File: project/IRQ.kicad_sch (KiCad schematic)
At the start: 6 parts, among them IC9 74HC148, SW5 NMI

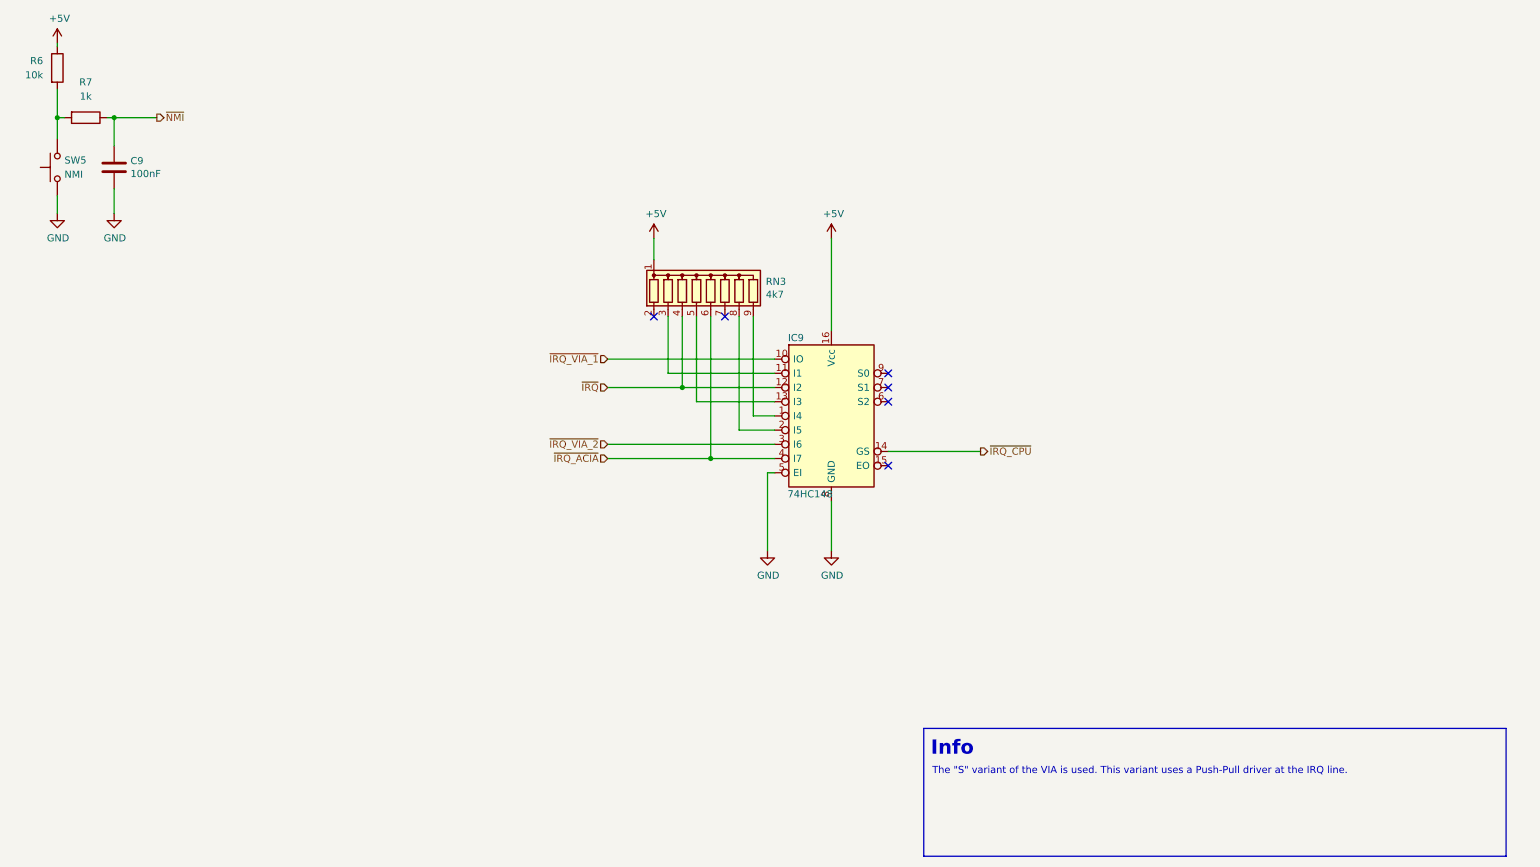
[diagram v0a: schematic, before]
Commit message: Fix grid issues, fix missing libraries, replace FT232 with FT231
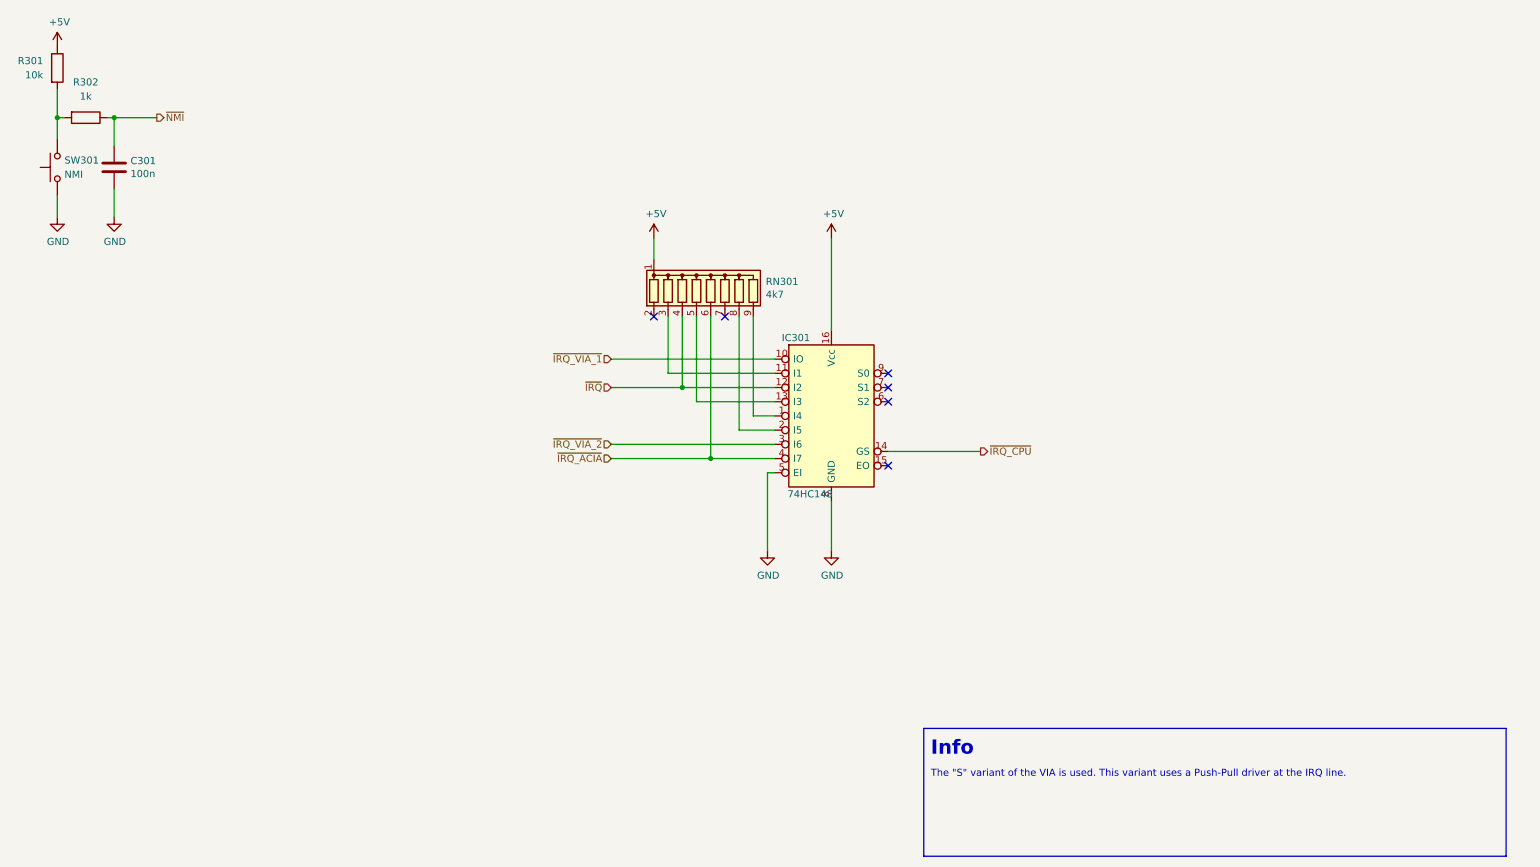
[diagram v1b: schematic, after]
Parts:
- C301: renamed from C9; value 100nF -> 100n
- renumbered IC9 to IC301, R6 to R301, R7 to R302, RN3 to RN301, SW5 to SW301

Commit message: Fix swapped DM and DP, add missing datasheets, remove Mouser property
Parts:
- C301: Mouser 810-FA18X8R1H104KRU6 -> (none)
- IC301: Mouser 595-SN74HC148N -> (none)
- R301: Mouser 603-MFP-25BRD52-10K -> (none)
- R302: Mouser 603-MFP-25BRD52-1K -> (none)
- RN301: Mouser 652-4609M-1LF-4.7K -> (none)
- SW301: Mouser 506-2-1825910-7 -> (none)
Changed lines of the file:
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@@
 			)
 		)
-		(property "Datasheet" "~"
+		(property "Datasheet" "https://www.mouser.de/datasheet/2/447/YAGEO_MFP_datasheet_2024v3-3447153.pdf"
 			(at 22.86 22.86 0)
 			(effects
@@
 		)
 		(property "Mfr. No." "MFP-25BRD52-10K"
-			(at 22.86 22.86 0)
-			(effects
-				(font
-					(size 1.27 1.27)
-				)
-				(hide yes)
-			)
-		)
-		(property "Mouser" "603-MFP-25BRD52-10K"
 			(at 22.86 22.86 0)
 			(effects
@@
 			)
 		)
-		(property "Datasheet" "~"
+		(property "Datasheet" "https://www.mouser.de/datasheet/2/418/7/ENG_CD_1825910_C10-2021098.pdf"
 			(at 17.78 40.64 0)
 			(effects
@@
 			)
 		)
-		(property "Mouser" "506-2-1825910-7"
-			(at 22.86 40.64 0)
-			(effects
-				(font
-					(size 1.27 1.27)
-				)
-				(hide yes)
-			)
-		)
 		(property "Distributor" "Mouser"
 			(at 22.86 40.64 0)
@@
 			)
 		)
-		(property "Datasheet" "~"
+		(property "Datasheet" "https://product.tdk.com/system/files/dam/doc/product/capacitor/ceramic/lead-mlcc/catalog/leadmlcc_halogenfree_fa150_en.pdf?ref_disty=mouser"
 			(at 33.02 40.64 0)
 			(effects
@@
 			)
 		)
-		(property "Mouser" "810-FA18X8R1H104KRU6"
-			(at 33.02 40.64 0)
-			(effects
-				(font
-					(size 1.27 1.27)
-				)
-				(hide yes)
-			)
-		)
 		(property "Distributor" "Mouser"
 			(at 33.02 40.64 0)
@@
 			)
 		)
-		(property "Mouser" "652-4609M-1LF-4.7K "
-			(at 139.7 62.23 0)
-			(effects
-				(font
-					(size 1.27 1.27)
-				)
-				(hide yes)
-			)
-		)
 		(property "Distributor" "Mouser"
 			(at 139.7 62.23 0)
@@
 		)
 		(property "Mfr. No." "SN74HC148N"
-			(at 161.29 85.09 0)
-			(effects
-				(font
-					(size 1.27 1.27)
-				)
-				(hide yes)
-			)
-		)
-		(property "Mouser" "595-SN74HC148N"
 			(at 161.29 85.09 0)
 			(effects
@@
 			)
 		)
-		(property "Datasheet" "~"
+		(property "Datasheet" "https://www.mouser.de/datasheet/2/447/Yageo_LR_MFP_1-1947926.pdf"
 			(at 27.94 31.75 0)
 			(effects
@@
 			(at 27.94 31.75 0)
 			(effects
-				(font
-					(size 1.27 1.27)
-				)
-				(hide yes)
-			)
-		)
-		(property "Mouser" "603-MFP-25BRD52-1K"
-			(at 27.94 31.75 0)
-			(effects
